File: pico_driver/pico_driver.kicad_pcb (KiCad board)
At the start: 4 copper layers, 65 x 56 mm, 25 parts, among them J1 GPIO, J2 SRV, J3 ESC, J4 ADC, J5 GP_Breakout, J6 VBUS_OUT, J7 3V3_OUT, J8 FUNC, SW1 OFF ON, SW2 SW_Push, SW3 SW_Push, U1 Pico

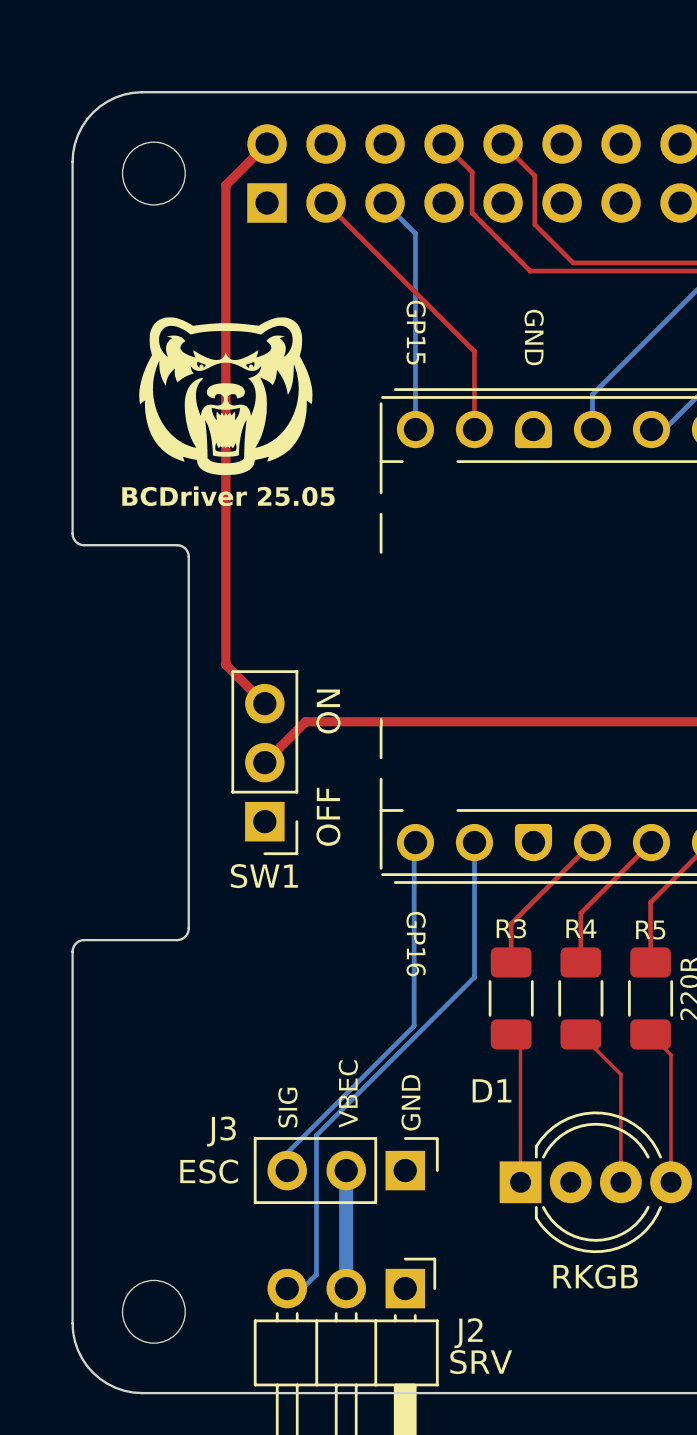
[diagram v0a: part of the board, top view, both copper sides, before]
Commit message: update esc and servo pin layout
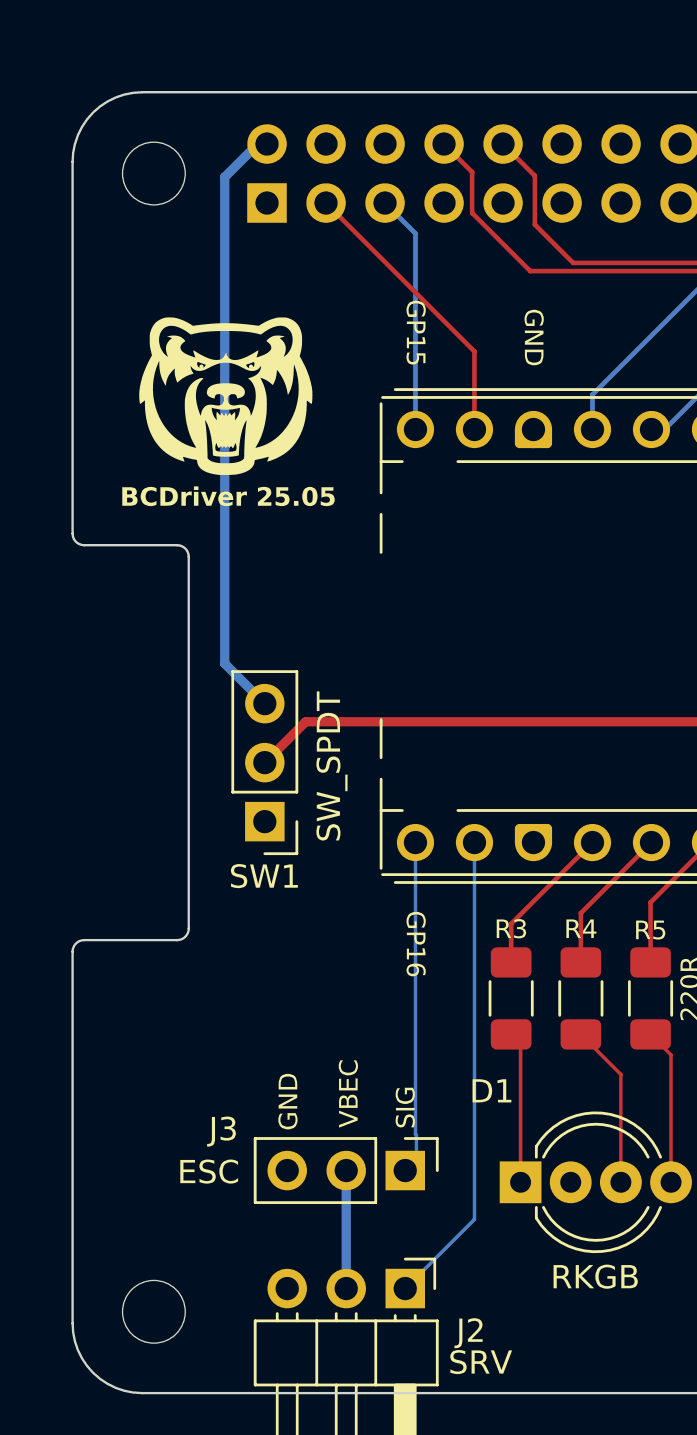
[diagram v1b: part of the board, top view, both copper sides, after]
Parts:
- SW1: value OFF ON -> SW_SPDT
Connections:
- J2 pad 1: GND -> /SERVO_SIG
- J2 pad 3: /SERVO_SIG -> GND
- J3 pad 1: GND -> /ESC_SIG
- J3 pad 3: /ESC_SIG -> GND
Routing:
- net /SERVO_SIG: track 22.9 -> 20.4 mm
- net /ESC_SIG: track 16.8 -> 14.3 mm
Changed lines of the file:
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@@
 			(layers "*.Cu" "*.Mask")
 			(remove_unused_layers no)
-			(net 1 "GND")
+			(net 38 "/ESC_SIG")
 			(pinfunction "Pin_1")
 			(pintype "passive")
@@
 			(layers "*.Cu" "*.Mask")
 			(remove_unused_layers no)
-			(net 38 "/ESC_SIG")
+			(net 1 "GND")
 			(pinfunction "Pin_3")
 			(pintype "passive")
@@
 			)
 		)
-		(property "Value" "OFF     ON"
+		(property "Value" "SW_SPDT"
 			(at -2.775 2.35 90)
 			(layer "F.SilkS")
@@
 			(layers "*.Cu" "*.Mask")
 			(remove_unused_layers no)
-			(net 1 "GND")
+			(net 37 "/SERVO_SIG")
 			(pinfunction "Pin_1")
 			(pintype "passive")
@@
 			(layers "*.Cu" "*.Mask")
 			(remove_unused_layers no)
-			(net 37 "/SERVO_SIG")
+			(net 1 "GND")
 			(pinfunction "Pin_3")
 			(pintype "passive")
@@
 	)
 	(gr_text "GND"
-		(at 114.6 87.5 90)
+		(at 109.3 87.45 90)
 		(layer "F.SilkS")
 		(effects
@@
 	)
 	(gr_text "SIG"
-		(at 109.3 87.7 90)
+		(at 114.35 87.7 90)
 		(layer "F.SilkS")
 		(effects
@@
 	)
 	(segment
-		(start 106.6 68.645)
-		(end 106.6 48)
+		(start 106.55 47.65)
+		(end 107.97 46.23)
 		(width 0.4)
-		(layer "F.Cu")
+		(layer "B.Cu")
 		(net 30)
 	)
 	(segment
-		(start 108.275 70.32)
-		(end 106.6 68.645)
+		(start 106.55 68.595)
+		(end 106.55 47.65)
 		(width 0.4)
-		(layer "F.Cu")
+		(layer "B.Cu")
 		(net 30)
 	)
 	(segment
-		(start 106.6 48)
+		(start 107.97 46.23)
 		(end 108.37 46.23)
 		(width 0.4)
-		(layer "F.Cu")
+		(layer "B.Cu")
+		(net 30)
+	)
+	(segment
+		(start 108.275 70.32)
+		(end 106.55 68.595)
+		(width 0.4)
+		(layer "B.Cu")
 		(net 30)
 	)
@@
 	)
 	(segment
-		(start 111.78 90.42)
-		(end 111.78 95.5)
-		(width 0.6)
+		(start 111.78 95.5)
+		(end 111.78 90.42)
+		(width 0.4)
 		(layer "B.Cu")
 		(net 36)
 	)
 	(segment
-		(start 117.3 76.3)
-		(end 117.3 82.1)
-		(width 0.2)
-		(layer "B.Cu")
-		(net 37)
-	)
-	(segment
-		(start 110.5 88.9)
-		(end 110.5 94.9)
-		(width 0.2)
-		(layer "B.Cu")
-		(net 37)
-	)
-	(segment
-		(start 117.3 82.1)
-		(end 110.5 88.9)
-		(width 0.2)
-		(layer "B.Cu")
-		(net 37)
-	)
-	(segment
-		(start 109.9 95.5)
-		(end 109.24 95.5)
-		(width 0.2)
+		(start 117.3 92.52)
+		(end 117.3 76.3)
+		(width 0.15)
 		(layer "B.Cu")
 		(net 37)
 	)
 	(segment
-		(start 110.5 94.9)
-		(end 109.9 95.5)
-		(width 0.2)
+		(start 114.32 95.5)
+		(end 117.3 92.52)
+		(width 0.15)
 		(layer "B.Cu")
 		(net 37)
 	)
 	(segment
-		(start 109.24 90.42)
-		(end 109.24 89.663612)
-		(width 0.2)
-		(layer "B.Cu")
-		(net 38)
-	)
-	(segment
-		(start 114.7 84.203612)
-		(end 114.7 76.36)
-		(width 0.2)
+		(start 114.32 90.42)
+		(end 114.8 89.94)
+		(width 0.15)
 		(layer "B.Cu")
 		(net 38)
 	)
 	(segment
-		(start 109.24 90.77)
-		(end 109.5 90.51)
-		(width 0.2)
+		(start 114.8 89.94)
+		(end 114.8 88.9)
+		(width 0.15)
 		(layer "B.Cu")
 		(net 38)
 	)
 	(segment
-		(start 114.7 76.36)
+		(start 114.76 88.86)
 		(end 114.76 76.3)
-		(width 0.2)
+		(width 0.15)
 		(layer "B.Cu")
 		(net 38)
 	)
 	(segment
-		(start 109.24 89.663612)
-		(end 114.7 84.203612)
-		(width 0.2)
+		(start 114.8 88.9)
+		(end 114.76 88.86)
+		(width 0.15)
 		(layer "B.Cu")
 		(net 38)

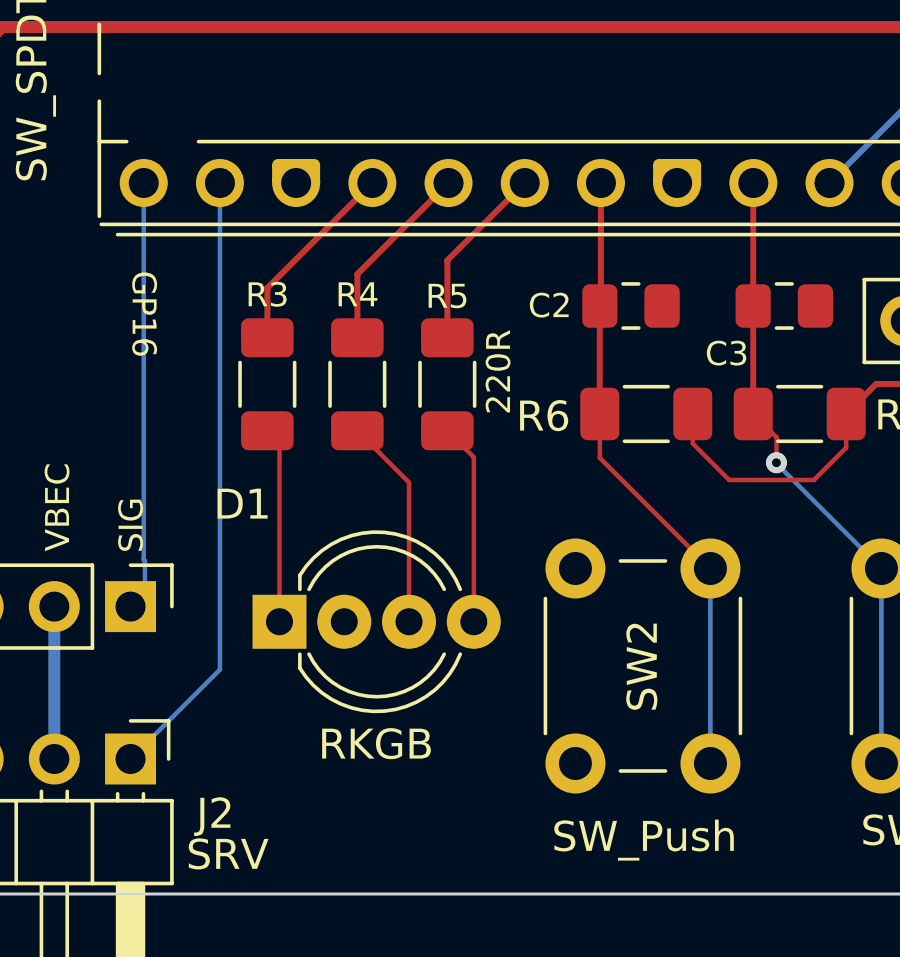
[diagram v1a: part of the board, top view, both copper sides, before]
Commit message: update LED footprint
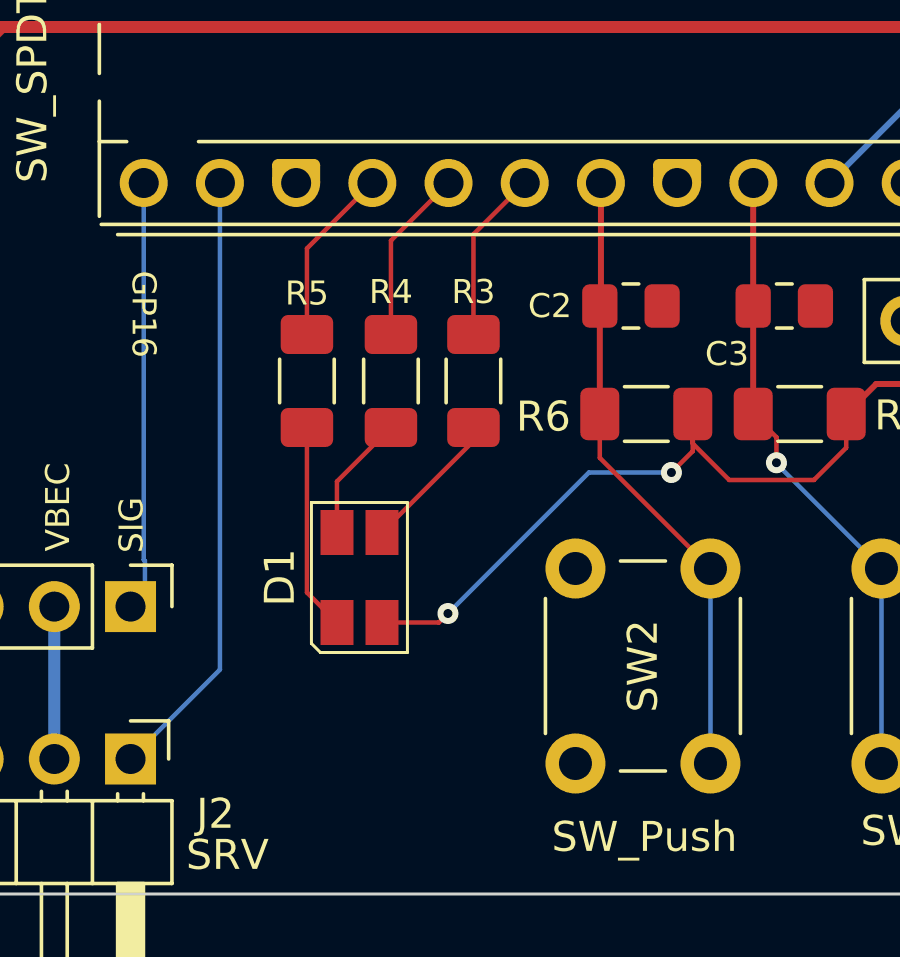
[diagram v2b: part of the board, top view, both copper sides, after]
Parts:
- D1: value RKGB -> ASMB-MTB1-0A3A2; footprint LED_THT:LED_D5.0mm-4_RGB_Wide_Pins -> LED_SMD:LED_Avago_PLCC4_3.2x2.8mm_CW
- moved R3 6.87 mm to (125.8, 82.9)
- moved R5 4.68 mm to (120.2, 82.9)
- moved D1 3.05 mm to (122.0, 89.5), turned to 90 degrees
- moved R4 1.13 mm to (123.0, 82.9)
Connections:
- D1 pad 1: Net-(D1-RA) -> Net-(D1-RK)
- D1 pad 2: GND -> Net-(D1-GK)
- D1 pad 3: Net-(D1-GA) -> Net-(D1-BK)
- D1 pad 4: Net-(D1-BA) -> 3V3_OUT
- R3 pad 1: Net-(D1-RA) -> Net-(D1-BK)
- R3 pad 2: /R_LED -> /B_LED
- R4 pad 1: Net-(D1-GA) -> Net-(D1-GK)
- R4 pad 2: /G_LED -> /R_LED
- R5 pad 1: Net-(D1-BA) -> Net-(D1-RK)
- R5 pad 2: /B_LED -> /G_LED
- U1 pad 24: /R_LED -> /G_LED
- U1 pad 25: /G_LED -> /R_LED
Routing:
- net 3V3_OUT: track 30.5 -> 43.6 mm, vias 0 -> 2
- net Net-(D1-GA): track 7.08 -> 0.00 mm
- net Net-(D1-RK): track 0.00 -> 6.91 mm
- net Net-(D1-BA): track 6.73 -> 0.00 mm
- net Net-(D1-RA): track 6.53 -> 0.00 mm
- net Net-(D1-BK): track 0.00 -> 4.76 mm
- net Net-(D1-GK): track 0.00 -> 4.25 mm
- net /R_LED: track 6.61 -> 5.85 mm

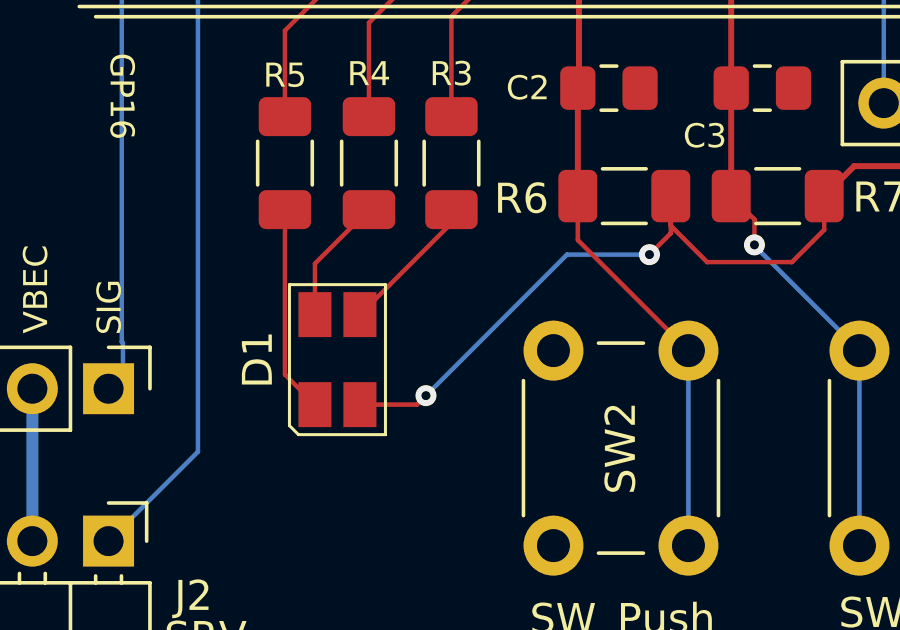
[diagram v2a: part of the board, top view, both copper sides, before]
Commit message: update rgb led footprint
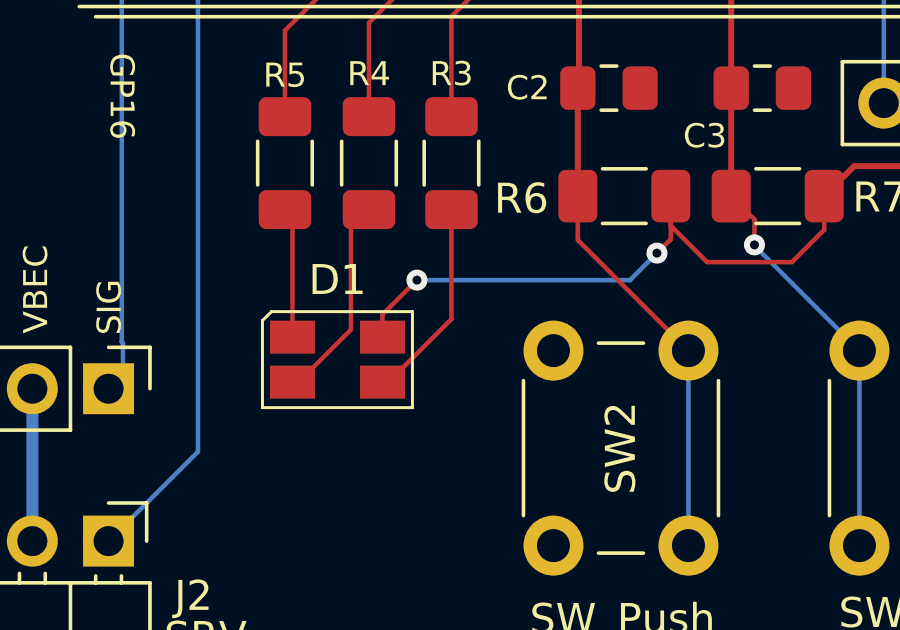
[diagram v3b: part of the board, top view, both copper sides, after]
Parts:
- turned D1 to 0 degrees
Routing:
- net Net-(D1-GK): track 4.25 -> 6.92 mm
- net Net-(D1-RK): track 6.91 -> 4.35 mm
- net Net-(D1-BK): track 4.76 -> 6.82 mm
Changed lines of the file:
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@@
 	(footprint "LED_SMD:LED_Avago_PLCC4_3.2x2.8mm_CW"
 		(layer "F.Cu")
-		(at 121.95 89.45 90)
+		(at 121.95 89.45)
 		(descr "3.2mm x 2.8mm PLCC4 RGB LED, https://docs.broadcom.com/docs/AV02-4186EN")
 		(tags "LED Avago PLCC-4 3528 ASMB-MTB0-0A3A2")
 		(property "Reference" "D1"
-			(at 0 -2.65 90)
+			(at 0 -2.65 0)
 			(layer "F.SilkS")
 			(effects
@@
 		)
 		(property "Value" "ASMB-MTB1-0A3A2"
-			(at 0 2.65 90)
+			(at 0 2.65 0)
 			(layer "F.Fab")
 			(effects
@@
 		)
 		(property "Datasheet" "https://docs.broadcom.com/docs/AV02-4194EN"
-			(at 0 0 90)
+			(at 0 0 0)
 			(unlocked yes)
 			(layer "F.Fab")
@@
 		)
 		(property "Description" "Tricolor Black Surface LED, Common Anode Pin 4, PLCC-4"
-			(at 0 0 90)
+			(at 0 0 0)
 			(unlocked yes)
 			(layer "F.Fab")
@@
 		(attr smd)
 		(fp_line
+			(start -2.5 1.6)
+			(end -2.5 -1.3)
+			(stroke
+				(width 0.1)
+				(type solid)
+			)
+			(layer "F.SilkS")
+		)
+		(fp_line
+			(start -2.5 1.6)
+			(end 2.5 1.6)
+			(stroke
+				(width 0.1)
+				(type solid)
+			)
+			(layer "F.SilkS")
+		)
+		(fp_line
+			(start -2.2 -1.6)
+			(end -2.5 -1.3)
+			(stroke
+				(width 0.1)
+				(type default)
+			)
+			(layer "F.SilkS")
+		)
+		(fp_line
 			(start -2.2 -1.6)
 			(end 2.5 -1.6)
@@
 		)
 		(fp_line
-			(start -2.2 -1.6)
-			(end -2.5 -1.3)
-			(stroke
-				(width 0.1)
-				(type default)
-			)
-			(layer "F.SilkS")
-		)
-		(fp_line
 			(start 2.5 1.6)
 			(end 2.5 -1.6)
@@
 		)
 		(fp_line
-			(start -2.5 1.6)
-			(end -2.5 -1.3)
-			(stroke
-				(width 0.1)
-				(type solid)
-			)
-			(layer "F.SilkS")
-		)
-		(fp_line
-			(start -2.5 1.6)
-			(end 2.5 1.6)
-			(stroke
-				(width 0.1)
-				(type solid)
-			)
-			(layer "F.SilkS")
+			(start -2.5 -1.65)
+			(end -2.5 1.65)
+			(stroke
+				(width 0.05)
+				(type solid)
+			)
+			(layer "F.CrtYd")
 		)
 		(fp_line
@@
 		)
 		(fp_line
-			(start -2.5 -1.65)
+			(start 2.5 1.65)
 			(end -2.5 1.65)
 			(stroke
@@
 		)
 		(fp_line
-			(start 2.5 1.65)
-			(end -2.5 1.65)
-			(stroke
-				(width 0.05)
-				(type solid)
-			)
-			(layer "F.CrtYd")
+			(start -1.6 -1.4)
+			(end -1.6 1.4)
+			(stroke
+				(width 0.1)
+				(type solid)
+			)
+			(layer "F.Fab")
+		)
+		(fp_line
+			(start -1.6 1.4)
+			(end 1.6 1.4)
+			(stroke
+				(width 0.1)
+				(type solid)
+			)
+			(layer "F.Fab")
+		)
+		(fp_line
+			(start -0.6 -1.4)
+			(end -1.6 -0.4)
+			(stroke
+				(width 0.1)
+				(type solid)
+			)
+			(layer "F.Fab")
 		)
 		(fp_line
@@
 		)
 		(fp_line
-			(start -0.6 -1.4)
-			(end -1.6 -0.4)
-			(stroke
-				(width 0.1)
-				(type solid)
-			)
-			(layer "F.Fab")
-		)
-		(fp_line
-			(start -1.6 -1.4)
-			(end -1.6 1.4)
-			(stroke
-				(width 0.1)
-				(type solid)
-			)
-			(layer "F.Fab")
-		)
-		(fp_line
 			(start 1.6 1.4)
 			(end 1.6 -1.4)
-			(stroke
-				(width 0.1)
-				(type solid)
-			)
-			(layer "F.Fab")
-		)
-		(fp_line
-			(start -1.6 1.4)
-			(end 1.6 1.4)
 			(stroke
 				(width 0.1)
@@
 		)
 		(fp_text user "${REFERENCE}"
-			(at 0 0 90)
+			(at 0 0 0)
 			(layer "F.Fab")
 			(effects
@@
 		)
 		(pad "1" smd rect
-			(at -1.5 -0.75 90)
+			(at -1.5 -0.75)
 			(size 1.5 1.1)
 			(layers "F.Cu" "F.Mask" "F.Paste")
@@
 		)
 		(pad "2" smd rect
-			(at 1.5 -0.75 90)
+			(at -1.5 0.75)
 			(size 1.5 1.1)
 			(layers "F.Cu" "F.Mask" "F.Paste")
@@
 		)
 		(pad "3" smd rect
-			(at 1.5 0.75 90)
+			(at 1.5 0.75)
 			(size 1.5 1.1)
 			(layers "F.Cu" "F.Mask" "F.Paste")
@@
 		)
 		(pad "4" smd rect
-			(at -1.5 0.75 90)
+			(at 1.5 -0.75)
 			(size 1.5 1.1)
 			(layers "F.Cu" "F.Mask" "F.Paste")
@@
 	)
 	(segment
-		(start 122.7 87.95)
-		(end 125.75 84.9)
+		(start 125.75 88.1)
+		(end 125.75 84.45)
 		(width 0.15)
 		(layer "F.Cu")
@@
 	)
 	(segment
-		(start 125.75 84.9)
-		(end 125.75 84.45)
+		(start 123.45 90.2)
+		(end 123.65 90.2)
+		(width 0.15)
+		(layer "F.Cu")
+		(net 39)
+	)
+	(segment
+		(start 123.65 90.2)
+		(end 125.75 88.1)
 		(width 0.15)
 		(layer "F.Cu")
@@
 	)
 	(segment
-		(start 121.2 86.25)
+		(start 120.45 90.2)
+		(end 120.65 90.2)
+		(width 0.15)
+		(layer "F.Cu")
+		(net 41)
+	)
+	(segment
+		(start 122.4 85.05)
 		(end 123 84.45)
 		(width 0.15)
@@
 	)
 	(segment
-		(start 121.2 87.95)
-		(end 121.2 86.25)
+		(start 120.65 90.2)
+		(end 122.4 88.45)
 		(width 0.15)
 		(layer "F.Cu")
@@
 	)
 	(segment
-		(start 120.2 89.95)
+		(start 122.4 88.45)
+		(end 122.4 85.05)
+		(width 0.15)
+		(layer "F.Cu")
+		(net 41)
+	)
+	(segment
+		(start 120.45 88.7)
+		(end 120.45 84.7)
+		(width 0.15)
+		(layer "F.Cu")
+		(net 42)
+	)
+	(segment
+		(start 120.45 84.7)
 		(end 120.2 84.45)
-		(width 0.15)
-		(layer "F.Cu")
-		(net 42)
-	)
-	(segment
-		(start 121.2 90.95)
-		(end 120.2 89.95)
 		(width 0.15)
 		(layer "F.Cu")
@@
 	)
 	(segment
-		(start 124.6 90.95)
-		(end 124.9 90.65)
-		(width 0.15)
-		(layer "F.Cu")
-		(net 54)
-	)
-	(segment
-		(start 133.0625 84.9)
-		(end 133.0625 84.9875)
+		(start 133.0625 84.9875)
+		(end 133.0625 84)
 		(width 0.15)
 		(layer "F.Cu")
@@
 		(start 134.275 86.2)
 		(end 137.1 86.2)
+		(width 0.15)
+		(layer "F.Cu")
+		(net 54)
+	)
+	(segment
+		(start 123.45 88.7)
+		(end 123.45 87.95)
 		(width 0.15)
 		(layer "F.Cu")
@@
 	)
 	(segment
-		(start 122.7 90.95)
-		(end 124.6 90.95)
+		(start 132.6 85.9)
+		(end 133.0625 85.4375)
 		(width 0.15)
 		(layer "F.Cu")
@@
 	)
 	(segment
-		(start 132.35 85.95)
-		(end 133.0625 85.2375)
+		(start 133.0625 85.4375)
+		(end 133.0625 84)
 		(width 0.15)
 		(layer "F.Cu")
@@
 	)
 	(segment
-		(start 133.0625 85.2375)
-		(end 133.0625 84.9)
-		(width 0.15)
-		(layer "F.Cu")
-		(net 54)
-	)
-	(segment
 		(start 133.0625 84.9875)
 		(end 134.275 86.2)
@@
 	)
 	(segment
-		(start 133.0625 84)
-		(end 133.0625 84.9)
+		(start 123.45 87.95)
+		(end 124.6 86.8)
 		(width 0.15)
 		(layer "F.Cu")
@@
 	)
 	(via
-		(at 124.9 90.65)
+		(at 124.6 86.8)
 		(size 0.7)
 		(drill 0.3)
@@
 	)
 	(via
-		(at 132.35 85.95)
+		(at 132.6 85.9)
 		(size 0.7)
 		(drill 0.3)
@@
 	)
 	(segment
-		(start 124.9 90.65)
-		(end 129.6 85.95)
+		(start 131.7 86.8)
+		(end 132.6 85.9)
 		(width 0.15)
 		(layer "B.Cu")
@@
 	)
 	(segment
-		(start 129.6 85.95)
-		(end 132.35 85.95)
-		(width 0.15)
-		(layer "B.Cu")
+		(start 124.6 86.8)
+		(end 131.7 86.8)
+		(width 0.15)
+		(layer "B.Cu")
